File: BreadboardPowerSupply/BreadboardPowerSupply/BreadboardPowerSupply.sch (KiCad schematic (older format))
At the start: 15 parts, among them J1 Barrel_Jack_Switch, J2 Conn_02x02_Odd_Even, J3 Conn_02x02_Odd_Even, SW1 SW_DPDT_x2, U1 LM7805_TO220

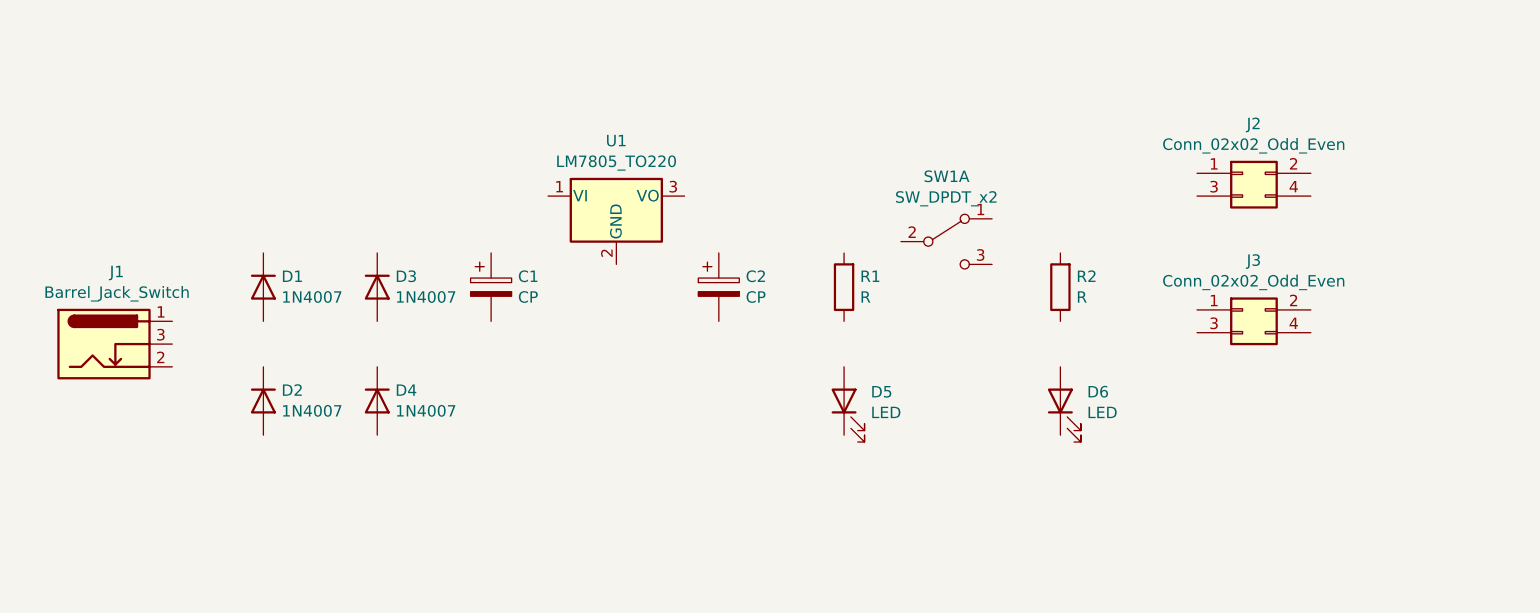
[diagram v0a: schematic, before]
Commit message: breadboard power supply
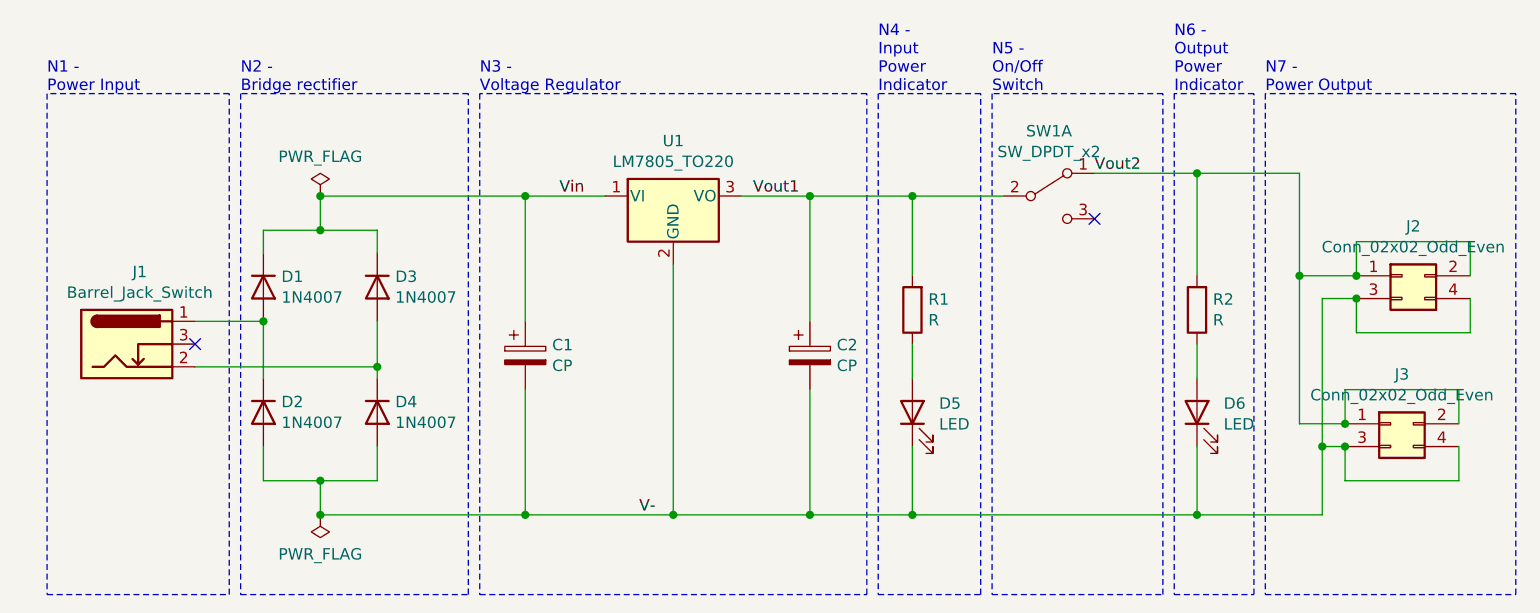
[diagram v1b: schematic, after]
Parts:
- C1: footprint Capacitor_THT:CP_Radial_D6.3mm_P2.50mm -> Capacitor_THT:CP_Radial_D10.0mm_P5.00mm
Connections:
- net Vin: now reaches U1.1 (VI)
- net Vin: now also C1.1, D1.1 (K), D3.1 (K)
- net V-: now reaches U1.2 (GND)
- net V-: now also C1.2, C2.2, D2.2 (A), D4.2 (A), D5.1 (K), D6.1 (K), J2.3 (Pin_3), J2.4 (Pin_4), J3.3 (Pin_3), J3.4 (Pin_4)
- net Vout1: now reaches U1.3 (VO)
- net Vout1: now also C2.1, R1.2, SW1.2 (B)
- net at D1.2 (A): now also D2.1 (K), J1.1
- net at D3.2 (A): now also D4.1 (K), J1.2
- net at D5.2 (A): now also R1.1
- net at D6.2 (A): now also R2.1
- net Vout2: now reaches R2.2
- net Vout2: now also J2.1 (Pin_1), J2.2 (Pin_2), J3.1 (Pin_1), J3.2 (Pin_2), SW1.1 (A)
- no-connect marks 0 -> 2
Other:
- note added: "N1 -\nPower Input"
- note added: "N2 - \nBridge rectifier"
- note added: "N3 - \nVoltage Regulator"
- note added: "N4 -\nInput\nPower\nIndicator"
- note added: "N5 - \nOn/Off\nSwitch"
- note added: "N6 -\nOutput\nPower\nIndicator"
- note added: "N7 - \nPower Output"
- moved on the sheet: C1, C2, D2, D4, D5, D6, J1, J2, J3, R1, R2, SW1A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

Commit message: no message
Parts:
- C1: value CP -> 470u
- C2: value CP -> 47u
- D1: Shop (none) -> https://si.farnell.com/multicomp-pro/1n4007/rectifier-singl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
- R1, R2: value R -> 220
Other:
- note added: "N4 -\nIN Power\nIndicator"
- note added: "N6 -\nOUT Power\nIndicator"
- note removed: "N4 -\nInput\nPower\nIndicator"
- note removed: "N6 -\nOutput\nPower\nIndicator"
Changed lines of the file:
@@
 EESchema Schematic File Version 4
-LIBS:BreadboardPowerSupply-cache
 EELAYER 30 0
 EELAYER END
@@
 Sheet 1 1
 Title "Breadboard Power Supply"
-Date "2019-11-30"
+Date "2020-10-18"
 Rev "v1"
 Comp ""
@@
 F 2 "Diode_THT:D_DO-41_SOD81_P10.16mm_Horizontal" H 3950 3775 50  0001 C CNN
 F 3 "http://www.vishay.com/docs/88503/1n4001.pdf" H 3950 3950 50  0001 C CNN
+F 4 "https://si.farnell.com/multicomp-pro/1n4007/rectifier-single-1a-1kv-do-204al/dp/2675796?st=1n4007" V 3950 3950 50  0001 C CNN "Shop"
 	1    3950 3950
 	0    1    1    0
@@
 P 5100 4250
 F 0 "C1" H 5218 4296 50  0000 L CNN
-F 1 "CP" H 5218 4205 50  0000 L CNN
+F 1 "470u" H 5218 4205 50  0000 L CNN
 F 2 "Capacitor_THT:CP_Radial_D10.0mm_P5.00mm" H 5138 4100 50  0001 C CNN
 F 3 "~" H 5100 4250 50  0001 C CNN
@@
 P 6350 4250
 F 0 "C2" H 6468 4296 50  0000 L CNN
-F 1 "CP" H 6468 4205 50  0000 L CNN
+F 1 "47u" H 6468 4205 50  0000 L CNN
 F 2 "Capacitor_THT:CP_Radial_D6.3mm_P2.50mm" H 6388 4100 50  0001 C CNN
 F 3 "~" H 6350 4250 50  0001 C CNN
@@
 P 6800 4050
 F 0 "R1" H 6730 4004 50  0000 R CNN
-F 1 "R" H 6730 4095 50  0000 R CNN
+F 1 "220" H 6730 4095 50  0000 R CNN
 F 2 "Resistor_THT:R_Axial_DIN0207_L6.3mm_D2.5mm_P7.62mm_Horizontal" V 6730 4050 50  0001 C CNN
 F 3 "~" H 6800 4050 50  0001 C CNN
@@
 P 8050 4050
 F 0 "R2" H 7980 4004 50  0000 R CNN
-F 1 "R" H 7980 4095 50  0000 R CNN
+F 1 "220" H 7980 4095 50  0000 R CNN
 F 2 "Resistor_THT:R_Axial_DIN0207_L6.3mm_D2.5mm_P7.62mm_Horizontal" V 7980 4050 50  0001 C CNN
 F 3 "~" H 8050 4050 50  0001 C CNN
@@
 N3 - \nVoltage Regulator
 Text Notes 6650 3100 0    50   ~ 0
-N4 -\nInput\nPower\nIndicator
+N4 -\nIN Power\nIndicator
 Text Notes 7150 3100 0    50   ~ 0
 N5 - \nOn/Off\nSwitch
 Text Notes 7950 3100 0    50   ~ 0
-N6 -\nOutput\nPower\nIndicator
-Text Notes 8350 3100 0    50   ~ 0
+N6 -\nOUT Power\nIndicator
+Text Notes 8450 3100 0    50   ~ 0
 N7 - \nPower Output
 Connection ~ 8600 4650
